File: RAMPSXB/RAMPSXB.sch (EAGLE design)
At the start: 97 parts, among them CN1 1X4-BIG, CN2 1X4-BIG, CN3 1X4-BIG, CN4 1X4-BIG, CN5 1X4-BIG, CN6 1X4-BIG, CN7 1X4-BIG, CN8 1X4-BIG, CN9 1X4-BIG, J1 1X2-3.5MM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

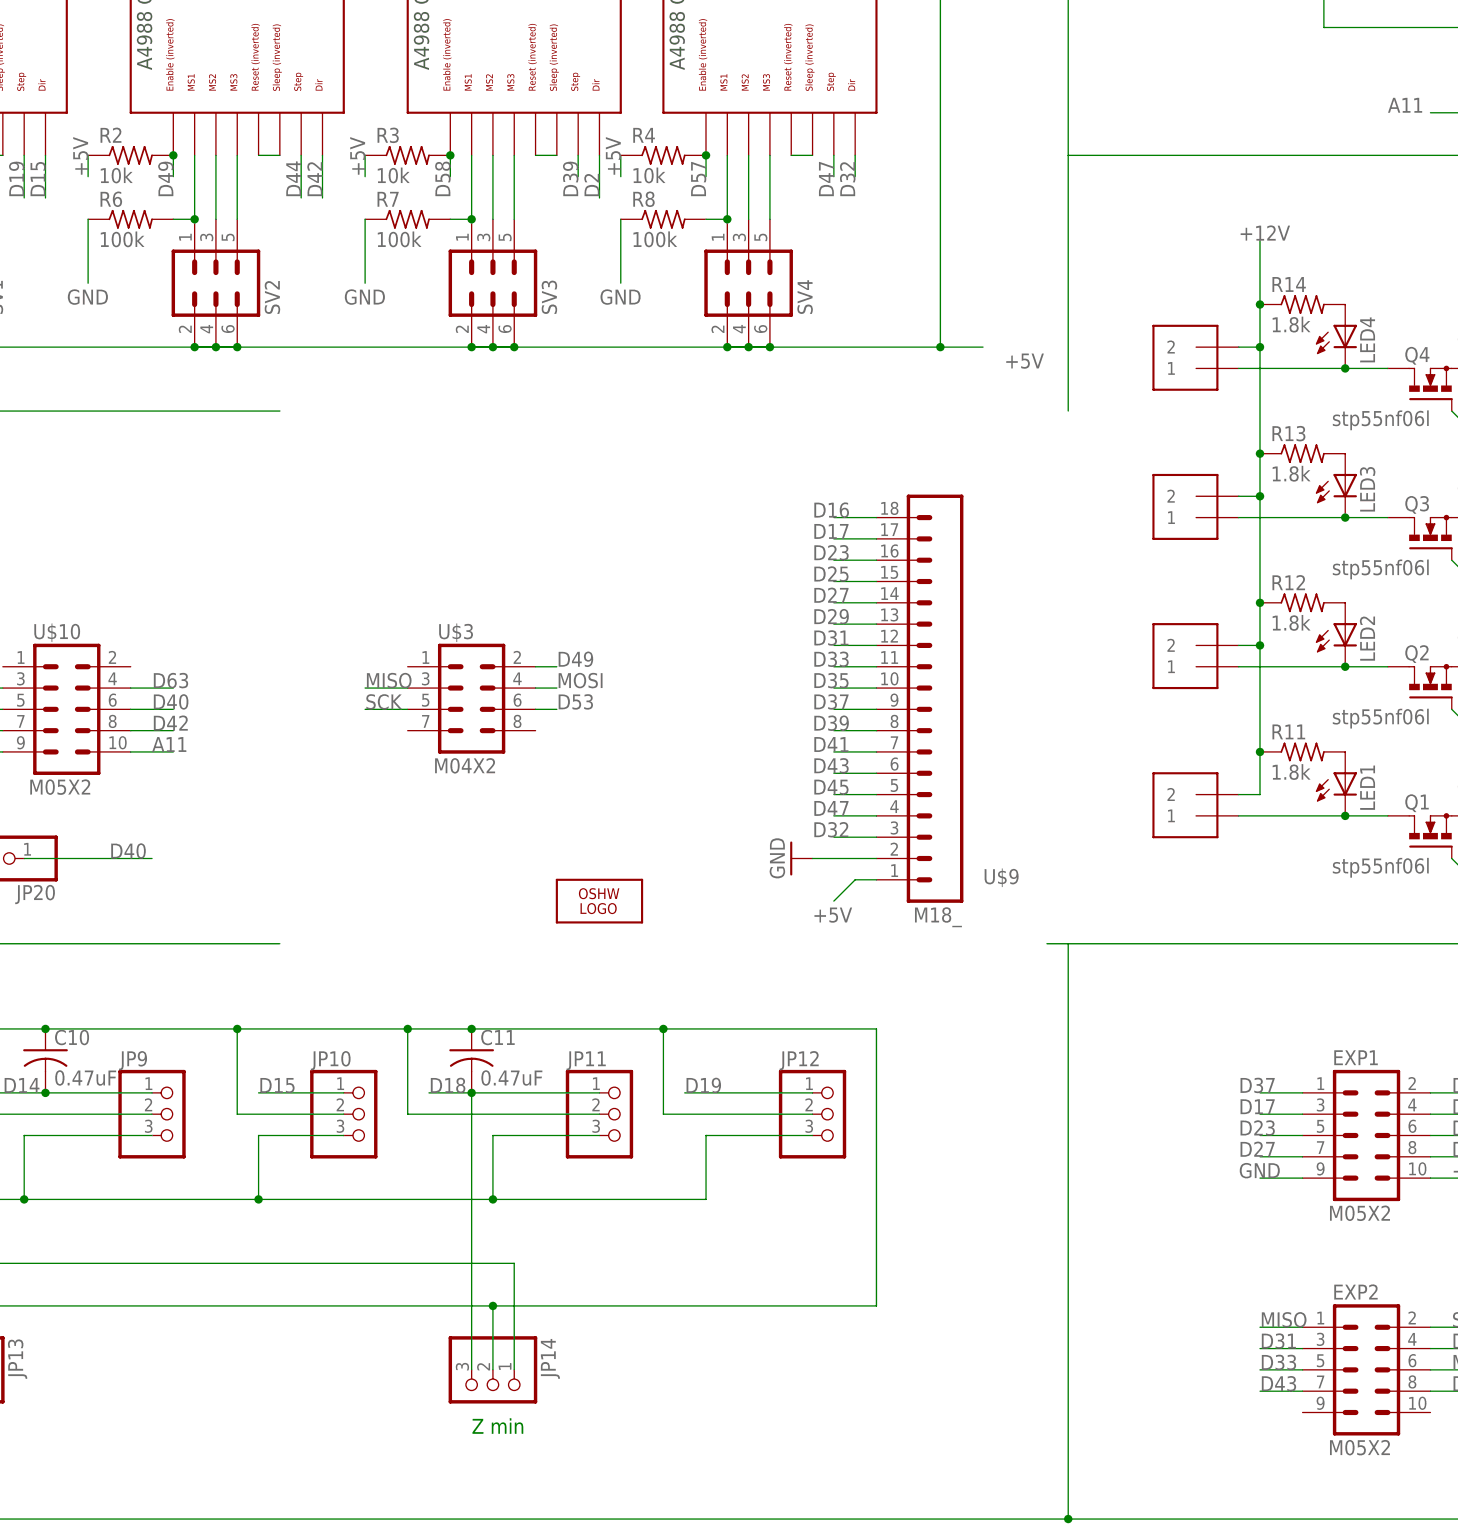
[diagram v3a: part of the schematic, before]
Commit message: Swapped pins 49 and 43. Documentation for the Smart Controller was incorrect.
Almost everything works, but the SD card for some reason opens, but I
cant read anything. Still working on that.
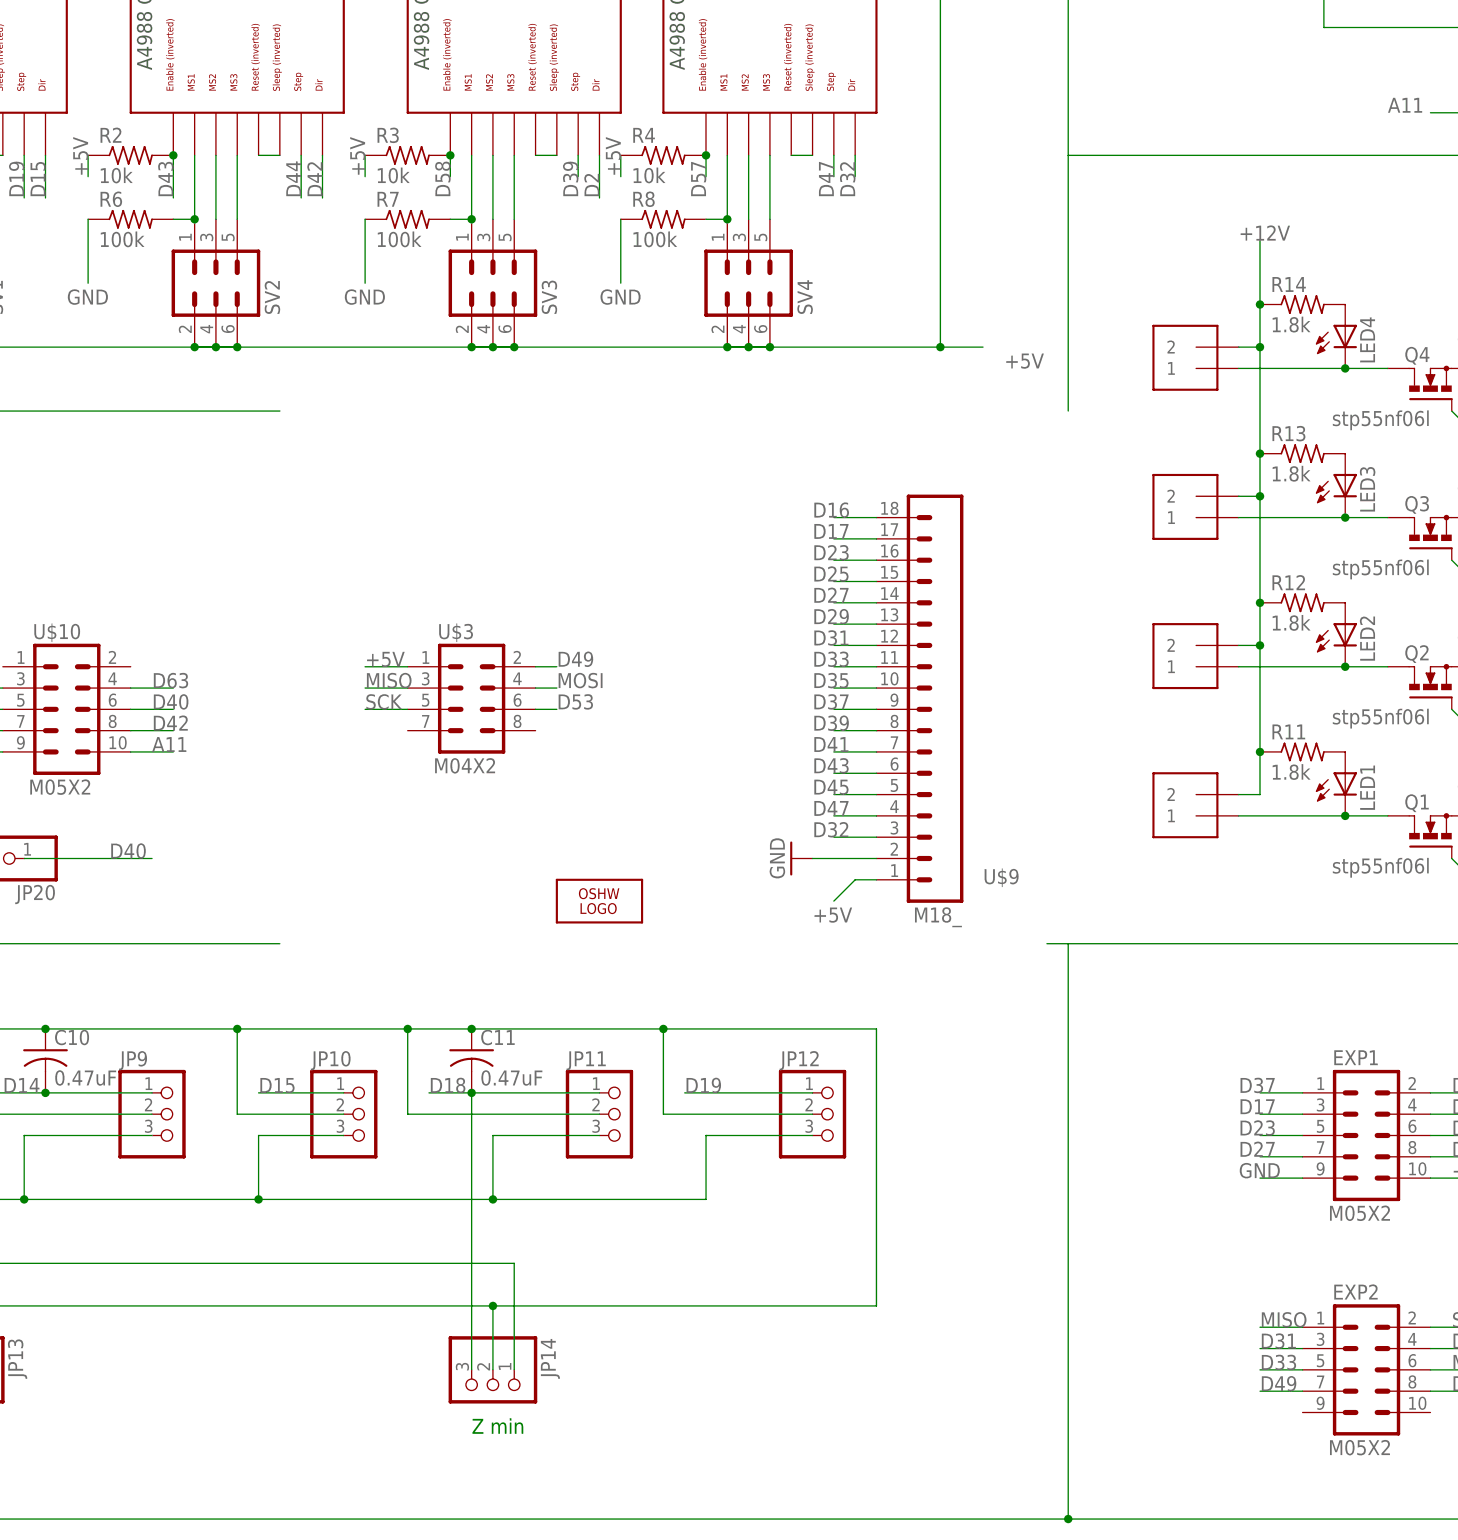
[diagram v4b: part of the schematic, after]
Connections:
- net +5V: now also U$3.1
- net D43: now also R2.2, U$2.EN; no longer EXP2.7
- net D49: now also EXP2.7; no longer R2.2, U$2.EN
